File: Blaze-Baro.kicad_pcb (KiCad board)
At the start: 2 copper layers, 0 parts

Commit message: all past changes to blaze baro
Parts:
- added C1: 100nF, Capacitor_SMD:C_0805_2012Metric, F.Cu at (102.2, 68.0)
- added R1: 10K, Resistor_SMD:R_0201_0603Metric, F.Cu at (101.2, 70.3)
- added R2: 10K, Resistor_SMD:R_0201_0603Metric, F.Cu at (101.2, 72.1)
- added U1: QTStemma_M, Avionics_Feet:0436500205, F.Cu at (94.5, 63.2)
- added U2: MS5611, Avionics_Feet:XDCR_MS561101BA03-50, F.Cu at (103.3, 63.2)

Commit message: push recent changes added stemma qt footprint
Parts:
- U1: footprint Avionics_Feet:0436500205 -> Connector_JST:JST_SH_SM04B-SRSS-TB_1x04-1MP_P1.00mm_Horizontal
- moved C1 18.6 mm to (94.0, 51.2)
- moved R2 17.6 mm to (95.7, 55.4)
- moved U2 15.6 mm to (88.8, 57.3)
- moved R1 14.8 mm to (94.7, 57.0)

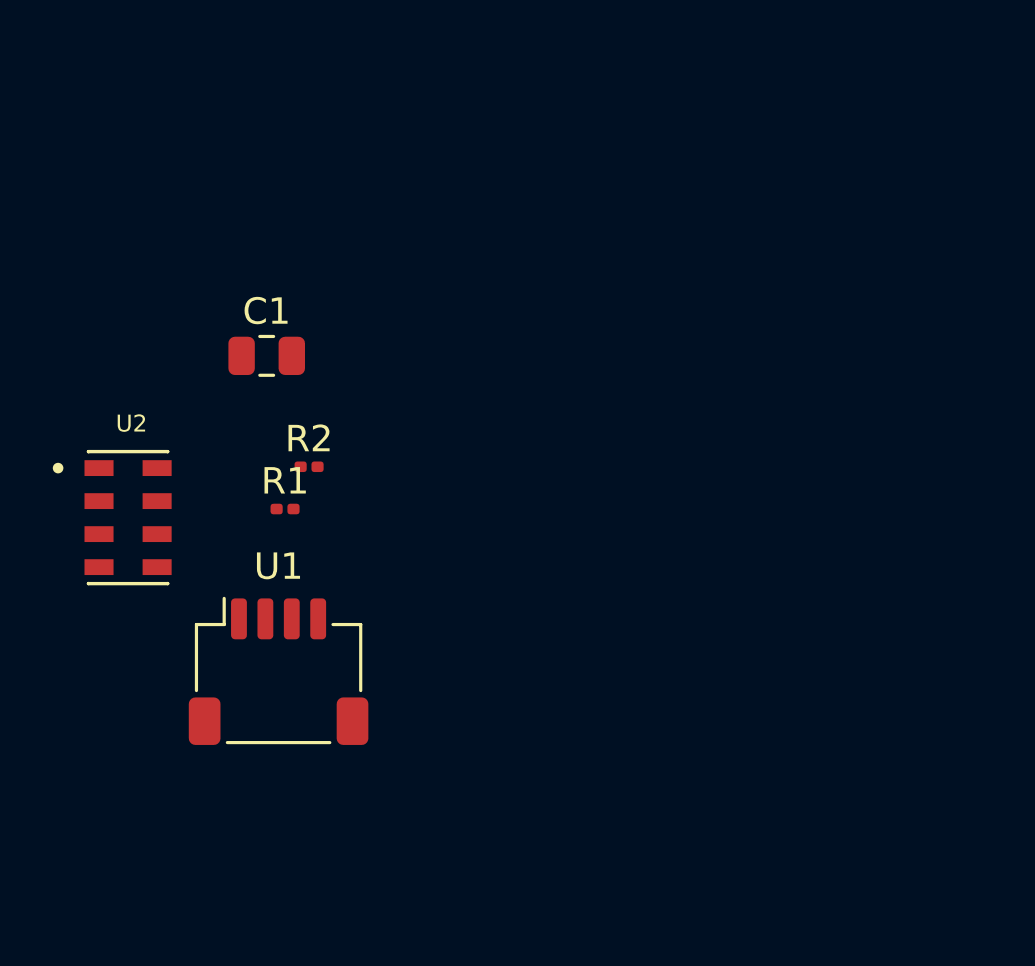
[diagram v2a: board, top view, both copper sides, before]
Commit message: Started work on pcb connections
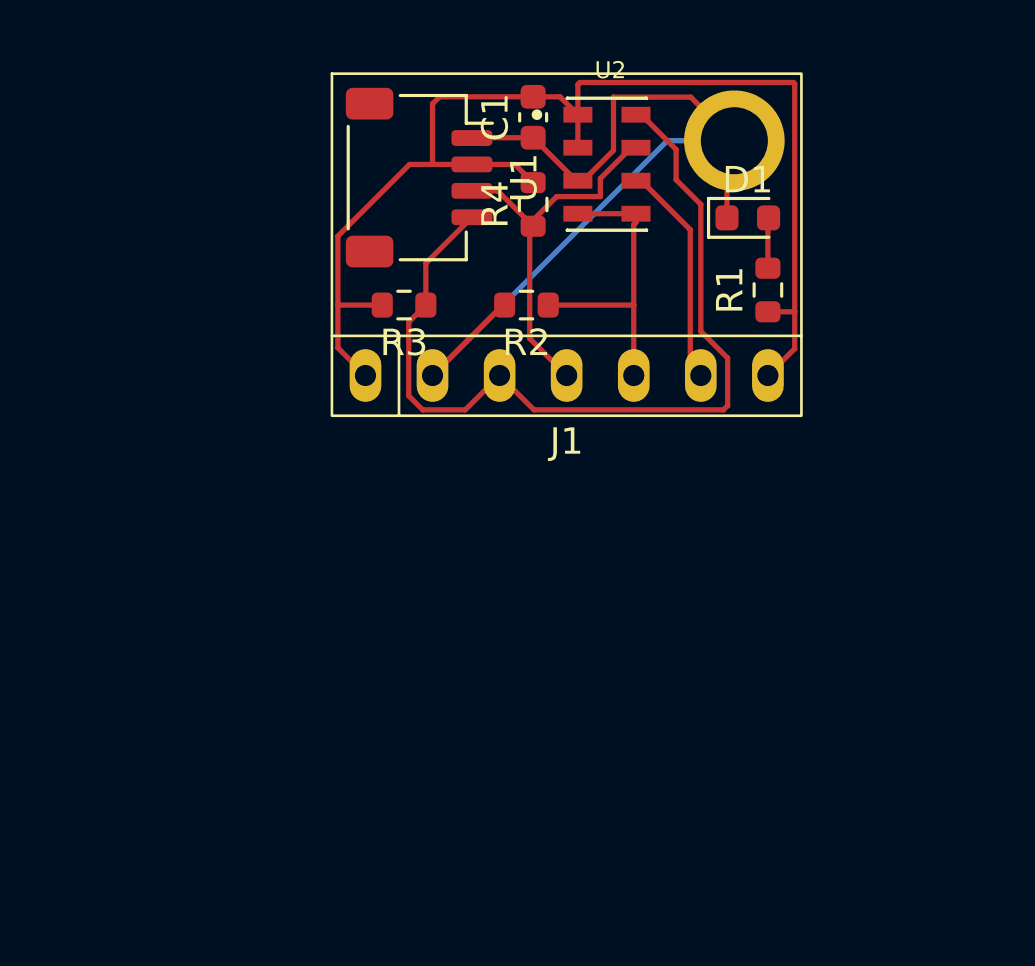
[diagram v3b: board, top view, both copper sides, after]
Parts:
- added D1: LED, LED_SMD:LED_0603_1608Metric, F.Cu at (112.3, 46.0)
- added J1: Pin Header, Avionics_Feet:MS5611, F.Cu at (105.4, 51.9)
- added R3: 1K, Resistor_SMD:R_0603_1608Metric, F.Cu at (99.3, 49.3)
- added R4: 1K, Resistor_SMD:R_0603_1608Metric, F.Cu at (104.1, 45.5)
- C1: value 100nF -> 1uF; footprint Capacitor_SMD:C_0805_2012Metric -> Capacitor_SMD:C_0603_1608Metric
- R1, R2: value 10K -> 1K; footprint Resistor_SMD:R_0201_0603Metric -> Resistor_SMD:R_0603_1608Metric
- moved U2 22.5 mm to (106.9, 43.9)
- moved R1 20.1 mm to (113.0, 48.7), turned to 90 degrees
- moved U1 19.5 mm to (99.8, 44.5), turned to -90 degrees
- moved C1 13.5 mm to (104.1, 42.2), turned to 90 degrees
- moved R2 10.3 mm to (103.9, 49.3), turned to 180 degrees
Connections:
- C1 pad 1: +3.3V -> GND
- R1 pad 2: /SDA -> Net-(D1-A)
- R2 pad 1: +3.3V -> /CSB
- R2 pad 2: /SCL -> GND
- U1 pad 1: +3.3V -> GND
- U2 pad 3: +3.3V -> GND
- U2 pad 4: +3.3V -> /CSB
- U2 pad 5: +3.3V -> /CSB
- U2 pad 6: unconnected-(U2-SDO-Pad6) -> /SDO
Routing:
- net +3.3V: track 0.00 -> 47.8 mm
- net GND: track 0.00 -> 36.6 mm
- net /SCL: track 0.00 -> 33.8 mm
- net /SDA: track 0.00 -> 14.8 mm
- net /CSB: track 0.00 -> 11.6 mm
- net /SDO: track 0.00 -> 8.51 mm
- net Net-(D1-A): track 0.00 -> 1.92 mm

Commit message: Closer to final PCB design
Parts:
- added R5: 4.7K, Resistor_SMD:R_0603_1608Metric, F.Cu at (117.9, 65.3)
- C1: value 1uF -> 0.1uF
- R3, R4: value 1K -> 4.7K
- moved C1 26.8 mm to (115.8, 66.3), turned to -90 degrees
- moved R4 23.0 mm to (113.8, 66.3)
- moved R2 22.6 mm to (119.9, 65.3), turned to 90 degrees
- moved D1 22.4 mm to (105.4, 67.3)
- moved R3 21.1 mm to (111.8, 66.3), turned to 90 degrees
- moved U1 19.1 mm to (106.2, 62.5)
- moved R1 19.0 mm to (109.0, 67.3), turned to 180 degrees
- moved J1 19.0 mm to (111.8, 69.8)
- moved U2 18.8 mm to (113.8, 61.5), turned to 180 degrees
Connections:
- J1 pad 7: +3.3V -> /PS
- U2 pad 2: +3.3V -> /PS
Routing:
- net /SCL: track 33.8 -> 12.7 mm
- net /CSB: track 11.6 -> 31.4 mm, vias 0 -> 2
- net /PS: track 0.00 -> 14.5 mm, vias 0 -> 1
- net +3.3V: track 47.8 -> 36.3 mm
- net GND: track 36.6 -> 46.1 mm
- net /SDO: track 8.51 -> 13.4 mm, vias 0 -> 1
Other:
- board outline added: 17.8 x 13 mm

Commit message: Finished design :)
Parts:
- added G***: LOGO, LOGO, B.Cu at (113.3, 63.2)
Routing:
- added copper zone on B.Cu, net (none)
- added copper zone on F.Cu, net (none)
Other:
- board text added: "CSB"
- board text added: "GND"
- board text added: "PS"
- board text added: "SCL"
- board text added: "SDA"
- board text added: "SDO"
- board text added: "UCSC"
- board text added: "VCC"

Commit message: Power net update
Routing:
- net GND: track 46.1 -> 0.00 mm, vias 0 -> 6
- net +3.3V: track 36.3 -> 32.3 mm, vias 0 -> 2
- added copper zone on B.Cu, net GND
- added copper zone on F.Cu, net GND
- removed copper zone on B.Cu, net (none)
- removed copper zone on F.Cu, net (none)
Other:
- board text added: "+3.3V ONLY!"

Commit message: Added i2c addr to silk
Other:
- board text added: "0x77"
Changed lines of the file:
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@@
 			(font
 				(size 1 1)
-				(thickness 0.1)
+				(thickness 0.125)
 			)
 			(justify left bottom mirror)
@@
 		(layer "B.SilkS")
 		(effects
+			(font
+				(size 0.5 0.5)
+				(thickness 0.1)
+				(bold yes)
+			)
+			(justify left bottom mirror)
+		)
+	)
+	(gr_text "0x77"
+		(at 107.569 61.468 0)
+		(layer "B.SilkS")
+		(effects
